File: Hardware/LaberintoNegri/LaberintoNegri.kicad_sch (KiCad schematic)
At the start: 22 parts

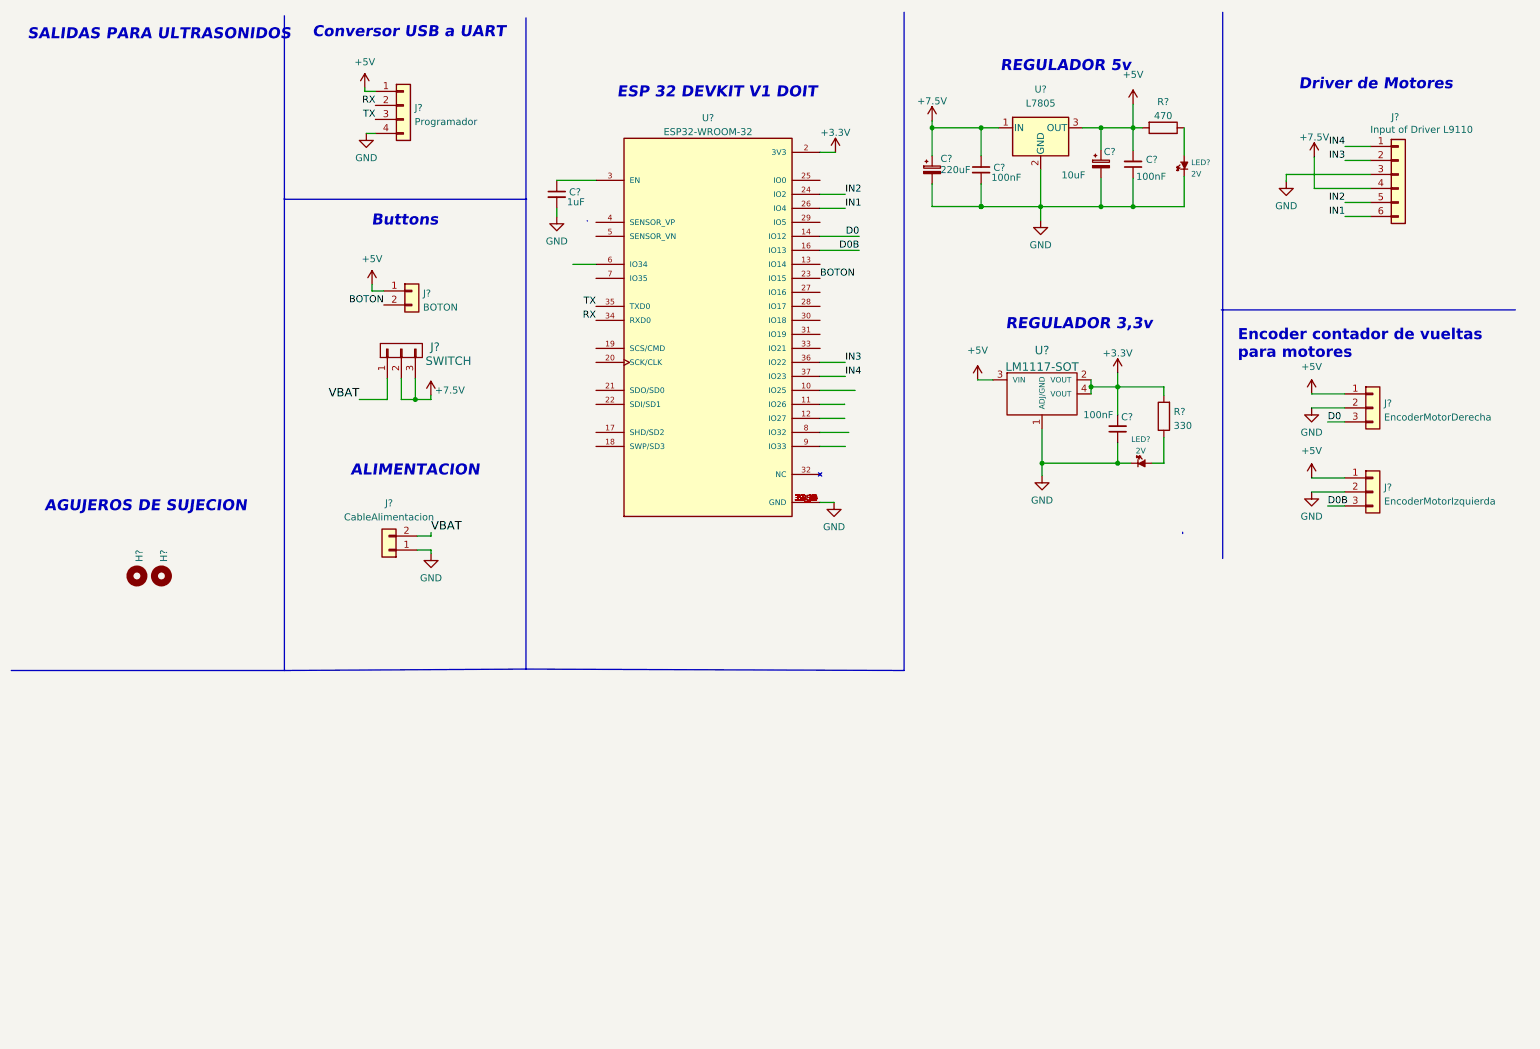
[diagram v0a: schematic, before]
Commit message: SENSORES IR SCH
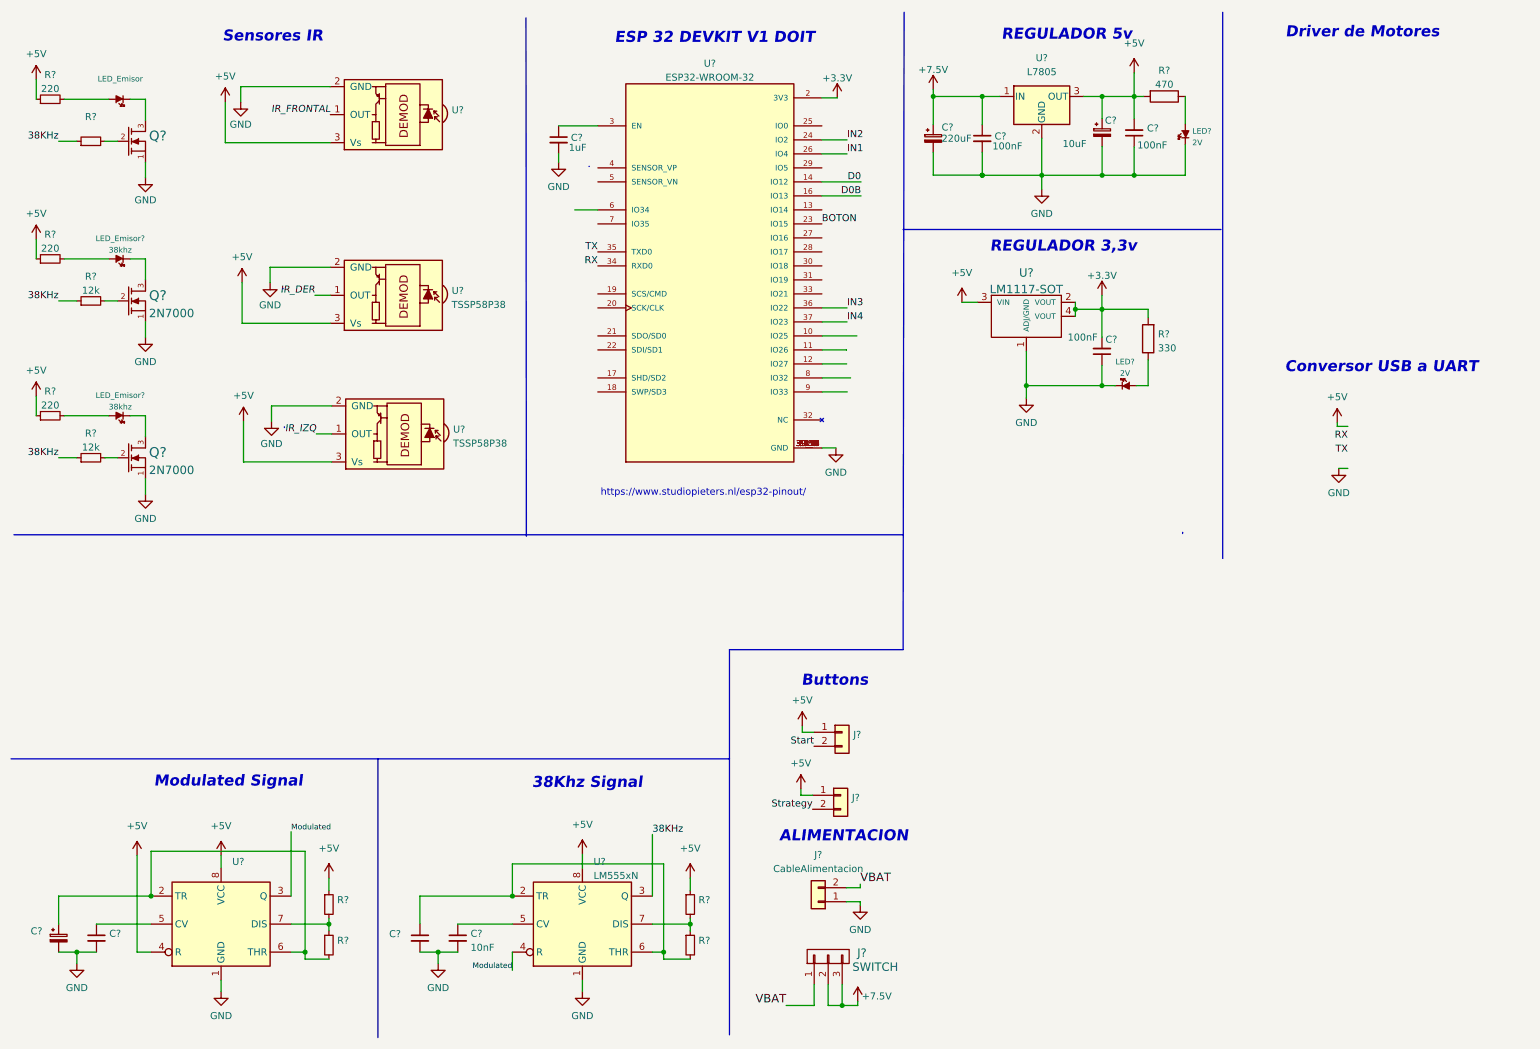
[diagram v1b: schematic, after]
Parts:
- removed H? (x2): Mounting_Hole, EESTN5:pad_2mm, symbol EESTN5:Mounting_Hole
- removed J?: Programador, EESTN5:pin_strip_4, symbol EESTN5:Conn_01x04
- removed J?: EncoderMotorIzquierda, EESTN5:Pin_Strip_3, symbol Connector_Generic:Conn_01x03
- removed J?: EncoderMotorDerecha, EESTN5:Pin_Strip_3, symbol Connector_Generic:Conn_01x03
- removed J?: Input of Driver L9110, EESTN5:Pin_Header_6, symbol Connector_Generic:Conn_01x06
- added C?: (no value), symbol Device:C_Polarized_Small
- added C? (x2): (no value), symbol Device:C_Small
- added C?: 10nF, symbol Device:C_Small
- added J?: (no value), Connector_PinSocket_2.54mm:PinSocket_1x02_P2.54mm_Vertical, symbol Connector_Generic:Conn_01x02
- added LED_Emisor: (no value), symbol EESTN5:LED
- added LED_Emisor? (x2): 38khz, symbol EESTN5:LED
- added Q? (x2): 2N7000, EESTN5:SOT23, symbol EESTN5:2N7000
- added Q?: (no value), symbol EESTN5:2N7000
- added R? (x5): (no value), symbol Device:R_Small
- added R? (x3): 220, symbol Device:R_Small
- added R? (x2): 12k, symbol Device:R_Small
- added U?: LM555xN, Package_DIP:DIP-8_W7.62mm, symbol Timer:LM555xN
- added U? (x2): TSSP58P38, OptoDevice:Vishay_MINICAST-3Pin, symbol Sensor_Proximity:TSSP58P38
- added U?: (no value), symbol Sensor_Proximity:TSSP58P38
- added U?: (no value), symbol Timer:LM555xN
- J?: value BOTON -> (none)
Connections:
- net +5V: now also J?.1 (Pin_1), R?.1, R?.1, R?.1, R?.1, R?.1, U?.3 (Vs), U?.3 (Vs), U?.3 (Vs), U?.4 (R), U?.8 (VCC), U?.8 (VCC)
- net BOTON: no longer J?.2 (Pin_2)
- net GND: now also C?.2, C?.2, C?.2, C?.2, Q?.1 (S), Q?.1 (S), Q?.1 (S), U?.1 (GND), U?.1 (GND), U?.2 (GND), U?.2 (GND), U?.2 (GND)
- new net: C?.1, R?.2, U?.2 (TR), U?.6 (THR) (x2)
- new net: R?.1, R?.2, U?.7 (DIS) (x2)
- new net: LED_Emisor?.1 (A), R?.2 (x2)
- new net: LED_Emisor.1 (A), R?.2
- new net: LED_Emisor.2 (K), Q?.3 (D)
- new net: C?.1, U?.5 (CV) (x2)
- new net: LED_Emisor?.2 (K), Q?.3 (D) (x2)
- new net: Q?.2 (G), R?.2 (x3)
- new net 38KHz: R?.1, R?.1, R?.1, U?.3 (Q)
- new net IR_DER: U?.1 (OUT)
- new net IR_FRONTAL: U?.1 (OUT)
- new net IR_IZQ: U?.1 (OUT)
- new net Modulated: U?.3 (Q), U?.4 (R)
- new net Start: J?.2 (Pin_2)
- new net Strategy: J?.2 (Pin_2)
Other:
- note added: "38Khz Signal"
- note added: "Modulated Signal"
- note added: "Sensores IR"
- note added: "https://www.studiopieters.nl/esp32-pinout/"
- note removed: "AGUJEROS DE SUJECION"
- note removed: "Encoder contador de vueltas para motores"
- note removed: "SALIDAS PARA ULTRASONIDOS"
- moved on the sheet: C?, J?, LED?, R?, U?
